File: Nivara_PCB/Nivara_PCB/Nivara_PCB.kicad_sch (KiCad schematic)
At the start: 21 parts, among them CN1 ANALOG_IN, CN2 RELAY, J1 AUXILIAR, P1 NPN_IN, P2 PNP_IN, P3 D_IN, P4 RUN/STOP, P5 NPN_OUT, P6 PNP_OUT, P7 RS485, P8 ANALOG_OUT., U1 2.54-2*2, U2 FUENTE IN

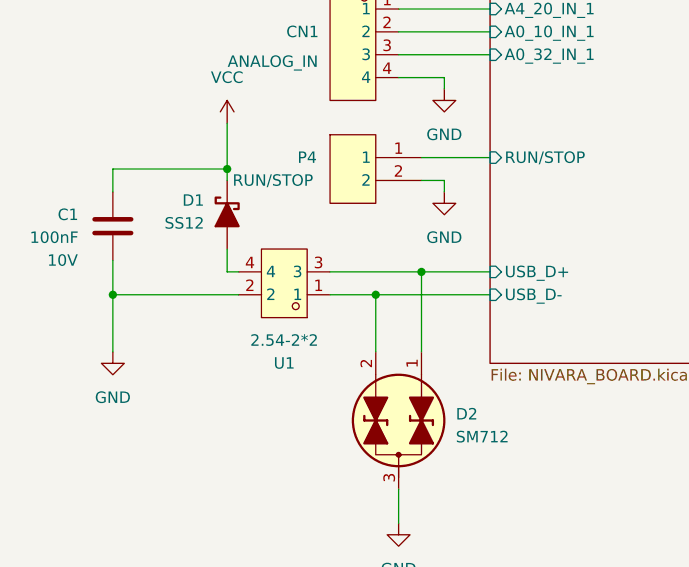
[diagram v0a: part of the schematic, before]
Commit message: Devolviendo los archivos eliminados sin querer a git.
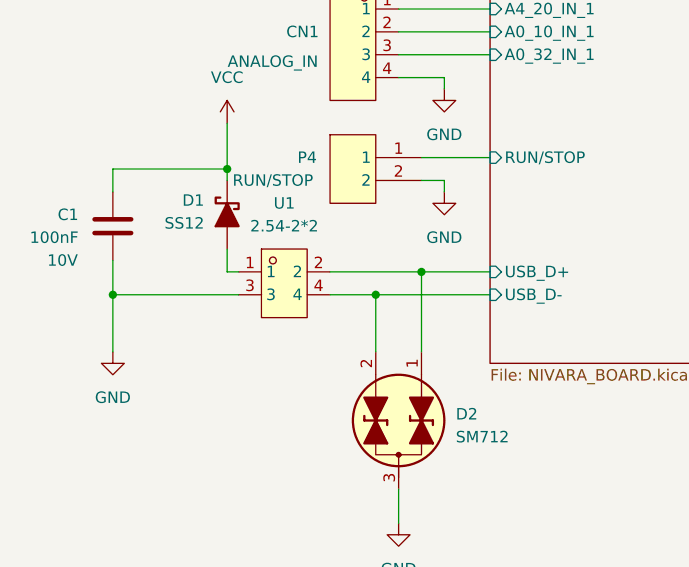
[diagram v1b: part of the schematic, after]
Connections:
- net GND: now also U1.3; no longer U1.2
- net NIVARA_BOARD/USB_D+: now also U1.2; no longer U1.3
- net NIVARA_BOARD/USB_D-: now also U1.4; no longer U1.1
- net at D1.2 (A): now also U1.1; no longer U1.4
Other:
- moved on the sheet: U1
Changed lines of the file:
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@@
 	(symbol
 		(lib_id "EasyEDA:2.54-2*2")
-		(at 50.8 120.65 180)
+		(at 50.8 120.65 0)
 		(unit 1)
 		(exclude_from_sim no)
@@
 		(on_board yes)
 		(dnp no)
+		(fields_autoplaced yes)
 		(property "Reference" "U1"
-			(at 50.8 129.54 0)
+			(at 50.8 111.76 0)
 			(effects
 				(font
@@
 		)
 		(property "Value" "2.54-2*2"
-			(at 50.8 127 0)
+			(at 50.8 114.3 0)
 			(effects
 				(font
@@
 		)
 		(property "Footprint" "Connector_PinHeader_2.54mm:PinHeader_2x02_P2.54mm_Vertical"
-			(at 50.8 111.76 0)
+			(at 50.8 129.54 0)
 			(effects
 				(font
@@
 		)
 		(property "LCSC Part" "C2977590"
-			(at 50.8 109.22 0)
+			(at 50.8 132.08 0)
 			(effects
 				(font

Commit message: Cambios en el diseño del pcb.
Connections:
- net GND: now also U1.2; no longer U1.3
- net NIVARA_BOARD/USB_D+: now also U1.3; no longer U1.2
- net NIVARA_BOARD/USB_D-: now also U1.1; no longer U1.4
- net at D1.2 (A): now also U1.4; no longer U1.1
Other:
- moved on the sheet: U1
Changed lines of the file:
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@@
 	(symbol
 		(lib_id "EasyEDA:2.54-2*2")
-		(at 50.8 120.65 0)
+		(at 50.8 120.65 180)
 		(unit 1)
 		(exclude_from_sim no)
@@
 		(on_board yes)
 		(dnp no)
-		(fields_autoplaced yes)
 		(property "Reference" "U1"
-			(at 50.8 111.76 0)
+			(at 50.8 129.54 0)
 			(effects
 				(font
@@
 		)
 		(property "Value" "2.54-2*2"
-			(at 50.8 114.3 0)
+			(at 50.8 127 0)
 			(effects
 				(font
@@
 		)
 		(property "Footprint" "Connector_PinHeader_2.54mm:PinHeader_2x02_P2.54mm_Vertical"
-			(at 50.8 129.54 0)
+			(at 50.8 111.76 0)
 			(effects
 				(font
@@
 		)
 		(property "LCSC Part" "C2977590"
-			(at 50.8 132.08 0)
+			(at 50.8 109.22 0)
 			(effects
 				(font
